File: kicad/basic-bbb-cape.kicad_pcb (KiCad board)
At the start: 2 copper layers, 54.6 x 86.4 mm, 4 parts, among them P1 BeagleBone_Black_Header, P2 BeagleBone_Black_Header, U1 CAT24C32YI-GT3

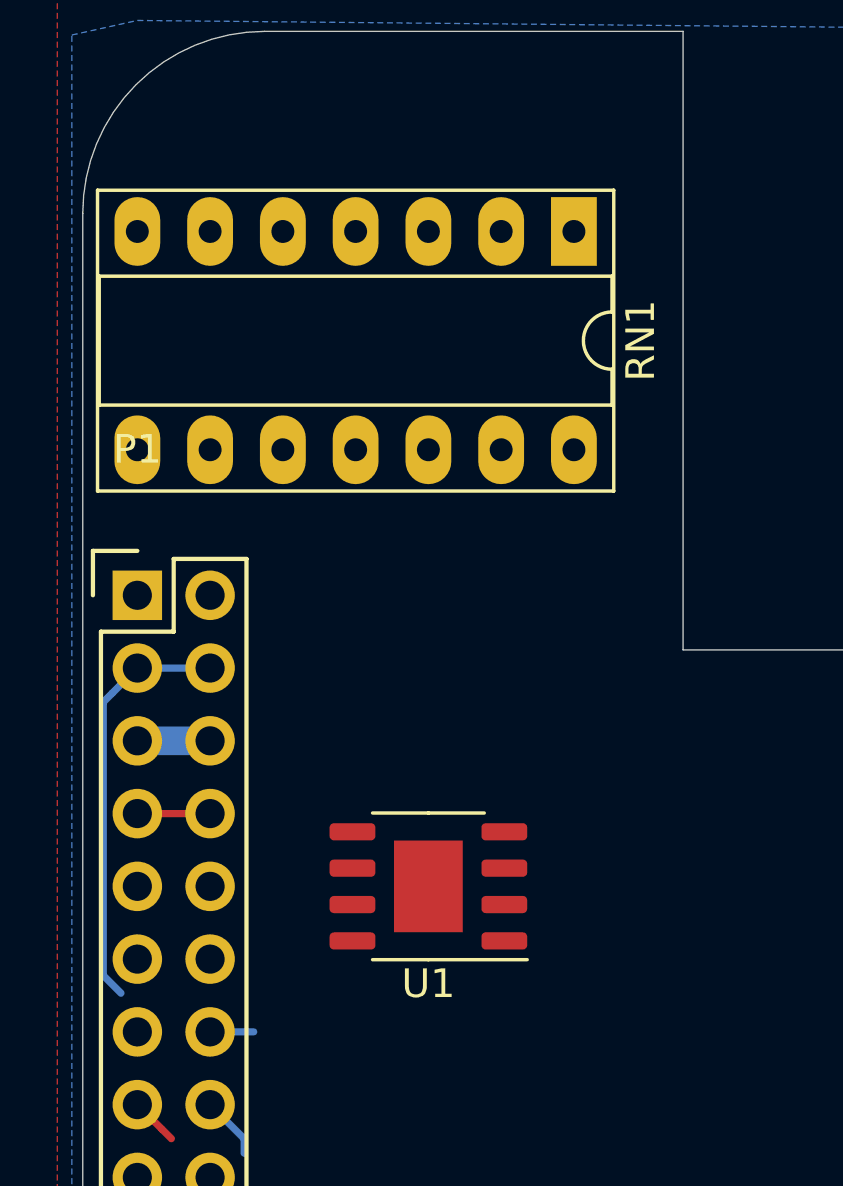
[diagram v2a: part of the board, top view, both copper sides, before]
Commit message: Rotate RP1 and U1 180 degrees
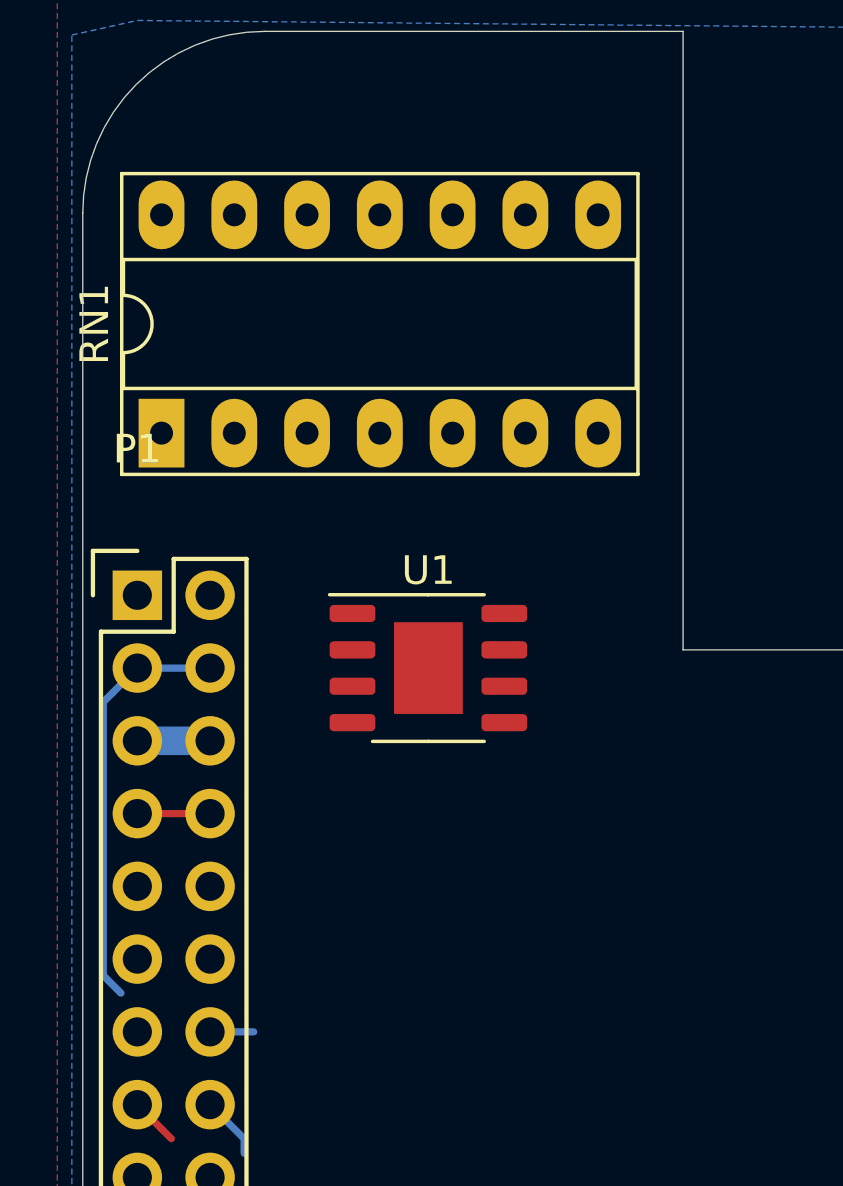
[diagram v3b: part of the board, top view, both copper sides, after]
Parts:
- moved RN1 16.0 mm to (117.2, 56.7), turned to 90 degrees
- moved U1 7.62 mm to (126.5, 64.9), turned to 0 degrees
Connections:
- RN1 pad 1: +3V3 -> Net-(JP1-Pad2)
- RN1 pad 10: Net-(RN1-Pad10) -> +3V3
- RN1 pad 11: unconnected-(RN1-Pad11) -> +3V3
- RN1 pad 12: Net-(RN1-Pad12) -> +3V3
- RN1 pad 13: Net-(JP2-Pad2) -> +3V3
- RN1 pad 14: Net-(JP1-Pad2) -> +3V3
- RN1 pad 2: +3V3 -> Net-(JP2-Pad2)
- RN1 pad 3: +3V3 -> Net-(RN1-Pad3)
- RN1 pad 4: +3V3 -> unconnected-(RN1-Pad4)
- RN1 pad 5: +3V3 -> Net-(RN1-Pad5)
- RN1 pad 6: +3V3 -> I2C2_SDA
- RN1 pad 7: +3V3 -> I2C2_SCL
- RN1 pad 8: I2C2_SDA -> +3V3
- RN1 pad 9: I2C2_SCL -> +3V3
- U1 pad 3: Net-(RN1-Pad12) -> Net-(RN1-Pad3)
- U1 pad 7: Net-(RN1-Pad10) -> Net-(RN1-Pad5)
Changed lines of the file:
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@@
   (net 83 "I2C2_SDA")
   (net 84 "I2C2_SCL")
-  (net 85 "Net-(RN1-Pad10)")
-  (net 86 "unconnected-(RN1-Pad11)")
-  (net 87 "Net-(RN1-Pad12)")
+  (net 85 "Net-(RN1-Pad3)")
+  (net 86 "unconnected-(RN1-Pad4)")
+  (net 87 "Net-(RN1-Pad5)")
   (net 88 "Net-(JP2-Pad2)")
   (net 89 "Net-(JP1-Pad2)")
@@
   )
   (footprint "Package_DIP:DIP-14_W7.62mm_Socket_LongPads" (layer "F.Cu")
-    (at 131.6101 49.6824 -90)
+    (at 117.2151 56.7224 90)
     (descr "14-lead though-hole mounted DIP package, row spacing 7.62 mm (300 mils), Socket, LongPads")
     (tags "THT DIP DIL PDIP 2.54mm 7.62mm 300mil Socket LongPads")
@@
     (fp_line (start 0.635 16.51) (end 0.635 -0.27) (layer "F.Fab") (width 0.1))
     (fp_line (start 0.635 -0.27) (end 1.635 -1.27) (layer "F.Fab") (width 0.1))
-    (pad "1" thru_hole rect (at 0 0 270) (size 2.4 1.6) (drill 0.8) (layers *.Cu *.Mask)
-      (net 1 "+3V3") (pinfunction "R1.1") (pintype "passive"))
-    (pad "2" thru_hole oval (at 0 2.54 270) (size 2.4 1.6) (drill 0.8) (layers *.Cu *.Mask)
-      (net 1 "+3V3") (pinfunction "R2.1") (pintype "passive"))
-    (pad "3" thru_hole oval (at 0 5.08 270) (size 2.4 1.6) (drill 0.8) (layers *.Cu *.Mask)
-      (net 1 "+3V3") (pinfunction "R3.1") (pintype "passive"))
-    (pad "4" thru_hole oval (at 0 7.62 270) (size 2.4 1.6) (drill 0.8) (layers *.Cu *.Mask)
-      (net 1 "+3V3") (pinfunction "R4.1") (pintype "passive"))
-    (pad "5" thru_hole oval (at 0 10.16 270) (size 2.4 1.6) (drill 0.8) (layers *.Cu *.Mask)
-      (net 1 "+3V3") (pinfunction "R5.1") (pintype "passive"))
-    (pad "6" thru_hole oval (at 0 12.7 270) (size 2.4 1.6) (drill 0.8) (layers *.Cu *.Mask)
-      (net 1 "+3V3") (pinfunction "R6.1") (pintype "passive"))
-    (pad "7" thru_hole oval (at 0 15.24 270) (size 2.4 1.6) (drill 0.8) (layers *.Cu *.Mask)
-      (net 1 "+3V3") (pinfunction "R7.1") (pintype "passive"))
-    (pad "8" thru_hole oval (at 7.62 15.24 270) (size 2.4 1.6) (drill 0.8) (layers *.Cu *.Mask)
-      (net 83 "I2C2_SDA") (pinfunction "R7.2") (pintype "passive"))
-    (pad "9" thru_hole oval (at 7.62 12.7 270) (size 2.4 1.6) (drill 0.8) (layers *.Cu *.Mask)
-      (net 84 "I2C2_SCL") (pinfunction "R6.2") (pintype "passive"))
-    (pad "10" thru_hole oval (at 7.62 10.16 270) (size 2.4 1.6) (drill 0.8) (layers *.Cu *.Mask)
-      (net 85 "Net-(RN1-Pad10)") (pinfunction "R5.2") (pintype "passive"))
-    (pad "11" thru_hole oval (at 7.62 7.62 270) (size 2.4 1.6) (drill 0.8) (layers *.Cu *.Mask)
-      (net 86 "unconnected-(RN1-Pad11)") (pinfunction "R4.2") (pintype "passive+no_connect"))
-    (pad "12" thru_hole oval (at 7.62 5.08 270) (size 2.4 1.6) (drill 0.8) (layers *.Cu *.Mask)
-      (net 87 "Net-(RN1-Pad12)") (pinfunction "R3.2") (pintype "passive"))
-    (pad "13" thru_hole oval (at 7.62 2.54 270) (size 2.4 1.6) (drill 0.8) (layers *.Cu *.Mask)
-      (net 88 "Net-(JP2-Pad2)") (pinfunction "R2.2") (pintype "passive"))
-    (pad "14" thru_hole oval (at 7.62 0 270) (size 2.4 1.6) (drill 0.8) (layers *.Cu *.Mask)
-      (net 89 "Net-(JP1-Pad2)") (pinfunction "R1.2") (pintype "passive"))
+    (pad "1" thru_hole rect (at 0 0 90) (size 2.4 1.6) (drill 0.8) (layers *.Cu *.Mask)
+      (net 89 "Net-(JP1-Pad2)") (pinfunction "R1.1") (pintype "passive"))
+    (pad "2" thru_hole oval (at 0 2.54 90) (size 2.4 1.6) (drill 0.8) (layers *.Cu *.Mask)
+      (net 88 "Net-(JP2-Pad2)") (pinfunction "R2.1") (pintype "passive"))
+    (pad "3" thru_hole oval (at 0 5.08 90) (size 2.4 1.6) (drill 0.8) (layers *.Cu *.Mask)
+      (net 85 "Net-(RN1-Pad3)") (pinfunction "R3.1") (pintype "passive"))
+    (pad "4" thru_hole oval (at 0 7.62 90) (size 2.4 1.6) (drill 0.8) (layers *.Cu *.Mask)
+      (net 86 "unconnected-(RN1-Pad4)") (pinfunction "R4.1") (pintype "passive"))
+    (pad "5" thru_hole oval (at 0 10.16 90) (size 2.4 1.6) (drill 0.8) (layers *.Cu *.Mask)
+      (net 87 "Net-(RN1-Pad5)") (pinfunction "R5.1") (pintype "passive"))
+    (pad "6" thru_hole oval (at 0 12.7 90) (size 2.4 1.6) (drill 0.8) (layers *.Cu *.Mask)
+      (net 83 "I2C2_SDA") (pinfunction "R6.1") (pintype "passive"))
+    (pad "7" thru_hole oval (at 0 15.24 90) (size 2.4 1.6) (drill 0.8) (layers *.Cu *.Mask)
+      (net 84 "I2C2_SCL") (pinfunction "R7.1") (pintype "passive"))
+    (pad "8" thru_hole oval (at 7.62 15.24 90) (size 2.4 1.6) (drill 0.8) (layers *.Cu *.Mask)
+      (net 1 "+3V3") (pinfunction "R7.2") (pintype "passive"))
+    (pad "9" thru_hole oval (at 7.62 12.7 90) (size 2.4 1.6) (drill 0.8) (layers *.Cu *.Mask)
+      (net 1 "+3V3") (pinfunction "R6.2") (pintype "passive"))
+    (pad "10" thru_hole oval (at 7.62 10.16 90) (size 2.4 1.6) (drill 0.8) (layers *.Cu *.Mask)
+      (net 1 "+3V3") (pinfunction "R5.2") (pintype "passive"))
+    (pad "11" thru_hole oval (at 7.62 7.62 90) (size 2.4 1.6) (drill 0.8) (layers *.Cu *.Mask)
+      (net 1 "+3V3") (pinfunction "R4.2") (pintype "passive"))
+    (pad "12" thru_hole oval (at 7.62 5.08 90) (size 2.4 1.6) (drill 0.8) (layers *.Cu *.Mask)
+      (net 1 "+3V3") (pinfunction "R3.2") (pintype "passive"))
+    (pad "13" thru_hole oval (at 7.62 2.54 90) (size 2.4 1.6) (drill 0.8) (layers *.Cu *.Mask)
+      (net 1 "+3V3") (pinfunction "R2.2") (pintype "passive"))
+    (pad "14" thru_hole oval (at 7.62 0 90) (size 2.4 1.6) (drill 0.8) (layers *.Cu *.Mask)
+      (net 1 "+3V3") (pinfunction "R1.2") (pintype "passive"))
     (model "${KICAD6_3DMODEL_DIR}/Package_DIP.3dshapes/DIP-14_W7.62mm_Socket.wrl"
       (offset (xyz 0 0 0))
@@
   )
   (footprint "Package_SO:HTSOP-8-1EP_3.9x4.9mm_P1.27mm_EP2.4x3.2mm" (layer "F.Cu")
-    (at 126.5301 72.5424 180)
+    (at 126.5301 64.9224)
     (descr "HTSOP, 8 Pin (https://media.digikey.com/pdf/Data%20Sheets/Rohm%20PDFs/BD9G341EFJ.pdf), generated with kicad-footprint-generator ipc_gullwing_generator.py")
     (tags "HTSOP SO")
@@
     (fp_line (start 1.95 -2.45) (end 1.95 2.45) (layer "F.Fab") (width 0.1))
     (fp_line (start -0.975 -2.45) (end 1.95 -2.45) (layer "F.Fab") (width 0.1))
-    (pad "" smd roundrect (at 0.6 -0.8 180) (size 0.97 1.29) (layers "F.Paste") (roundrect_rratio 0.25))
-    (pad "" smd roundrect (at -0.6 -0.8 180) (size 0.97 1.29) (layers "F.Paste") (roundrect_rratio 0.25))
-    (pad "" smd roundrect (at 0.6 0.8 180) (size 0.97 1.29) (layers "F.Paste") (roundrect_rratio 0.25))
-    (pad "" smd roundrect (at -0.6 0.8 180) (size 0.97 1.29) (layers "F.Paste") (roundrect_rratio 0.25))
-    (pad "1" smd roundrect (at -2.65 -1.905 180) (size 1.6 0.6) (layers "F.Cu" "F.Paste" "F.Mask") (roundrect_rratio 0.25)
+    (pad "" smd roundrect (at 0.6 -0.8) (size 0.97 1.29) (layers "F.Paste") (roundrect_rratio 0.25))
+    (pad "" smd roundrect (at -0.6 -0.8) (size 0.97 1.29) (layers "F.Paste") (roundrect_rratio 0.25))
+    (pad "" smd roundrect (at 0.6 0.8) (size 0.97 1.29) (layers "F.Paste") (roundrect_rratio 0.25))
+    (pad "" smd roundrect (at -0.6 0.8) (size 0.97 1.29) (layers "F.Paste") (roundrect_rratio 0.25))
+    (pad "1" smd roundrect (at -2.65 -1.905) (size 1.6 0.6) (layers "F.Cu" "F.Paste" "F.Mask") (roundrect_rratio 0.25)
       (net 89 "Net-(JP1-Pad2)") (pinfunction "A0") (pintype "input"))
-    (pad "2" smd roundrect (at -2.65 -0.635 180) (size 1.6 0.6) (layers "F.Cu" "F.Paste" "F.Mask") (roundrect_rratio 0.25)
+    (pad "2" smd roundrect (at -2.65 -0.635) (size 1.6 0.6) (layers "F.Cu" "F.Paste" "F.Mask") (roundrect_rratio 0.25)
       (net 88 "Net-(JP2-Pad2)") (pinfunction "A1") (pintype "input"))
-    (pad "3" smd roundrect (at -2.65 0.635 180) (size 1.6 0.6) (layers "F.Cu" "F.Paste" "F.Mask") (roundrect_rratio 0.25)
-      (net 87 "Net-(RN1-Pad12)") (pinfunction "A2") (pintype "input"))
-    (pad "4" smd roundrect (at -2.65 1.905 180) (size 1.6 0.6) (layers "F.Cu" "F.Paste" "F.Mask") (roundrect_rratio 0.25)
+    (pad "3" smd roundrect (at -2.65 0.635) (size 1.6 0.6) (layers "F.Cu" "F.Paste" "F.Mask") (roundrect_rratio 0.25)
+      (net 85 "Net-(RN1-Pad3)") (pinfunction "A2") (pintype "input"))
+    (pad "4" smd roundrect (at -2.65 1.905) (size 1.6 0.6) (layers "F.Cu" "F.Paste" "F.Mask") (roundrect_rratio 0.25)
       (net 90 "GNDD") (pinfunction "GND") (pintype "power_in"))
-    (pad "5" smd roundrect (at 2.65 1.905 180) (size 1.6 0.6) (layers "F.Cu" "F.Paste" "F.Mask") (roundrect_rratio 0.25)
+    (pad "5" smd roundrect (at 2.65 1.905) (size 1.6 0.6) (layers "F.Cu" "F.Paste" "F.Mask") (roundrect_rratio 0.25)
       (net 83 "I2C2_SDA") (pinfunction "SDA") (pintype "bidirectional"))
-    (pad "6" smd roundrect (at 2.65 0.635 180) (size 1.6 0.6) (layers "F.Cu" "F.Paste" "F.Mask") (roundrect_rratio 0.25)
+    (pad "6" smd roundrect (at 2.65 0.635) (size 1.6 0.6) (layers "F.Cu" "F.Paste" "F.Mask") (roundrect_rratio 0.25)
       (net 84 "I2C2_SCL") (pinfunction "SCL") (pintype "input"))
-    (pad "7" smd roundrect (at 2.65 -0.635 180) (size 1.6 0.6) (layers "F.Cu" "F.Paste" "F.Mask") (roundrect_rratio 0.25)
-      (net 85 "Net-(RN1-Pad10)") (pinfunction "WP") (pintype "input"))
-    (pad "8" smd roundrect (at 2.65 -1.905 180) (size 1.6 0.6) (layers "F.Cu" "F.Paste" "F.Mask") (roundrect_rratio 0.25)
+    (pad "7" smd roundrect (at 2.65 -0.635) (size 1.6 0.6) (layers "F.Cu" "F.Paste" "F.Mask") (roundrect_rratio 0.25)
+      (net 87 "Net-(RN1-Pad5)") (pinfunction "WP") (pintype "input"))
+    (pad "8" smd roundrect (at 2.65 -1.905) (size 1.6 0.6) (layers "F.Cu" "F.Paste" "F.Mask") (roundrect_rratio 0.25)
       (net 1 "+3V3") (pinfunction "VCC") (pintype "power_in"))
-    (pad "9" smd rect (at 0 0 180) (size 2.4 3.2) (layers "F.Cu" "F.Mask"))
+    (pad "9" smd rect (at 0 0) (size 2.4 3.2) (layers "F.Cu" "F.Mask"))
     (model "${KICAD6_3DMODEL_DIR}/Package_SO.3dshapes/HTSOP-8-1EP_3.9x4.9mm_P1.27mm_EP2.4x3.2mm.wrl"
       (offset (xyz 0 0 0))

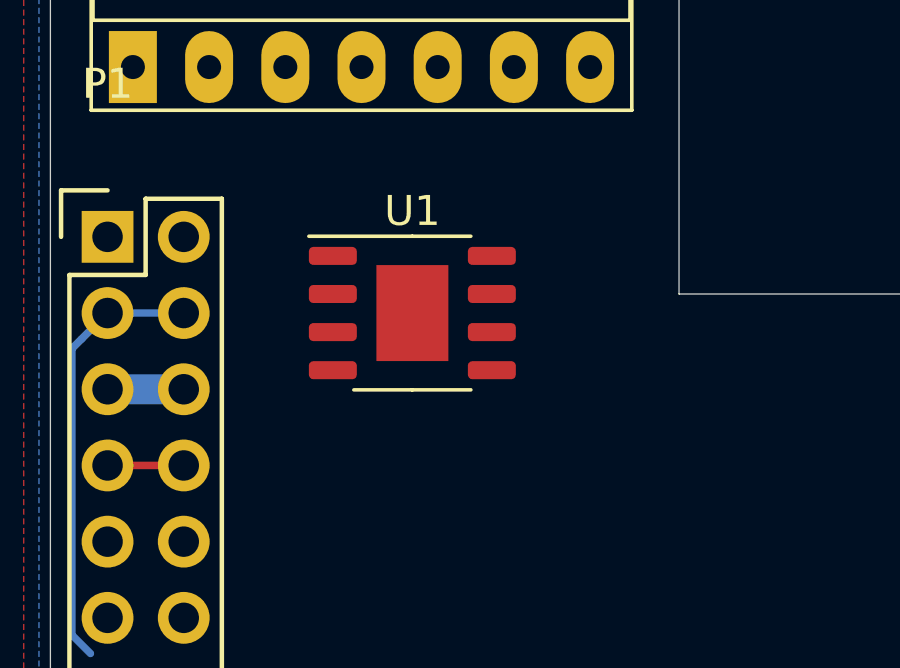
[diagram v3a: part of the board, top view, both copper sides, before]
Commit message: Add solder jumper to PCB
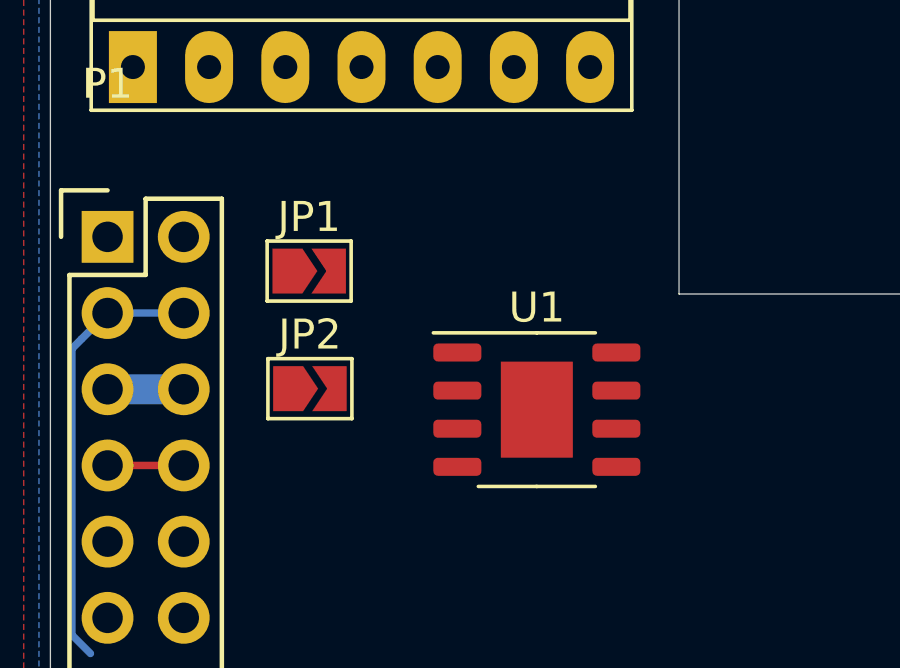
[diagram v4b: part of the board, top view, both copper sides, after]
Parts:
- added JP1: SolderJumper_2_Open, Jumper:SolderJumper-2_P1.3mm_Open_TrianglePad1.0x1.5mm, F.Cu at (123.1, 63.5)
- added JP2: SolderJumper_2_Open, Jumper:SolderJumper-2_P1.3mm_Open_TrianglePad1.0x1.5mm, F.Cu at (123.1, 67.4)
- moved U1 5.25 mm to (130.7, 68.1)
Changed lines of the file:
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@@
     )
+  )
+  (footprint "Jumper:SolderJumper-2_P1.3mm_Open_TrianglePad1.0x1.5mm" (layer "F.Cu")
+    (at 123.1151 67.4424)
+    (descr "SMD Solder Jumper, 1x1.5mm Triangular Pads, 0.3mm gap, open")
+    (tags "solder jumper open")
+    (property "Sheetfile" "basic-bbb-cape.kicad_sch")
+    (property "Sheetname" "")
+    (attr exclude_from_pos_files)
+    (fp_text reference "JP2" (at 0 -1.8) (layer "F.SilkS")
+      (effects (font (size 1 1) (thickness 0.15)))
+    )
+    (fp_text value "SolderJumper_2_Open" (at 0 1.9) (layer "F.Fab") hide
+      (effects (font (size 1 1) (thickness 0.15)))
+    )
+    (fp_line (start -1.4 1) (end -1.4 -1) (layer "F.SilkS") (width 0.12))
+    (fp_line (start 1.4 1) (end -1.4 1) (layer "F.SilkS") (width 0.12))
+    (fp_line (start -1.4 -1) (end 1.4 -1) (layer "F.SilkS") (width 0.12))
+    (fp_line (start 1.4 -1) (end 1.4 1) (layer "F.SilkS") (width 0.12))
+    (fp_line (start 1.65 1.25) (end 1.65 -1.25) (layer "F.CrtYd") (width 0.05))
+    (fp_line (start 1.65 1.25) (end -1.65 1.25) (layer "F.CrtYd") (width 0.05))
+    (fp_line (start -1.65 -1.25) (end -1.65 1.25) (layer "F.CrtYd") (width 0.05))
+    (fp_line (start -1.65 -1.25) (end 1.65 -1.25) (layer "F.CrtYd") (width 0.05))
+    (pad "1" smd custom (at -0.725 0) (size 0.3 0.3) (layers "F.Cu" "F.Mask")
+      (net 90 "GNDD") (pinfunction "A") (pintype "passive") (zone_connect 2)
+      (options (clearance outline) (anchor rect))
+      (primitives
+        (gr_poly (pts
+            (xy 1 0)
+            (xy 0.5 0.75)
+            (xy -0.5 0.75)
+            (xy -0.5 -0.75)
+            (xy 0.5 -0.75)
+          ) (width 0) (fill yes))
+      ))
+    (pad "2" smd custom (at 0.725 0) (size 0.3 0.3) (layers "F.Cu" "F.Mask")
+      (net 88 "Net-(JP2-Pad2)") (pinfunction "B") (pintype "passive") (zone_connect 2)
+      (options (clearance outline) (anchor rect))
+      (primitives
+        (gr_poly (pts
+            (xy 0.5 0.75)
+            (xy -0.65 0.75)
+            (xy -0.15 0)
+            (xy -0.65 -0.75)
+            (xy 0.5 -0.75)
+          ) (width 0) (fill yes))
+      ))
   )
   (footprint "Package_DIP:DIP-14_W7.62mm_Socket_LongPads" (layer "F.Cu")
@@
       (net 85 "Net-(RN1-Pad3)") (pinfunction "R3.1") (pintype "passive"))
     (pad "4" thru_hole oval (at 0 7.62 90) (size 2.4 1.6) (drill 0.8) (layers *.Cu *.Mask)
-      (net 86 "unconnected-(RN1-Pad4)") (pinfunction "R4.1") (pintype "passive"))
+      (net 86 "unconnected-(RN1-Pad4)") (pinfunction "R4.1") (pintype "passive+no_connect"))
     (pad "5" thru_hole oval (at 0 10.16 90) (size 2.4 1.6) (drill 0.8) (layers *.Cu *.Mask)
       (net 87 "Net-(RN1-Pad5)") (pinfunction "R5.1") (pintype "passive"))
@@
     )
   )
+  (footprint "Jumper:SolderJumper-2_P1.3mm_Open_TrianglePad1.0x1.5mm" (layer "F.Cu")
+    (at 123.0901 63.5224)
+    (descr "SMD Solder Jumper, 1x1.5mm Triangular Pads, 0.3mm gap, open")
+    (tags "solder jumper open")
+    (property "Sheetfile" "basic-bbb-cape.kicad_sch")
+    (property "Sheetname" "")
+    (attr exclude_from_pos_files)
+    (fp_text reference "JP1" (at 0 -1.8) (layer "F.SilkS")
+      (effects (font (size 1 1) (thickness 0.15)))
+    )
+    (fp_text value "SolderJumper_2_Open" (at 0 1.9) (layer "F.Fab") hide
+      (effects (font (size 1 1) (thickness 0.15)))
+    )
+    (fp_line (start 1.4 -1) (end 1.4 1) (layer "F.SilkS") (width 0.12))
+    (fp_line (start 1.4 1) (end -1.4 1) (layer "F.SilkS") (width 0.12))
+    (fp_line (start -1.4 1) (end -1.4 -1) (layer "F.SilkS") (width 0.12))
+    (fp_line (start -1.4 -1) (end 1.4 -1) (layer "F.SilkS") (width 0.12))
+    (fp_line (start -1.65 -1.25) (end 1.65 -1.25) (layer "F.CrtYd") (width 0.05))
+    (fp_line (start 1.65 1.25) (end -1.65 1.25) (layer "F.CrtYd") (width 0.05))
+    (fp_line (start 1.65 1.25) (end 1.65 -1.25) (layer "F.CrtYd") (width 0.05))
+    (fp_line (start -1.65 -1.25) (end -1.65 1.25) (layer "F.CrtYd") (width 0.05))
+    (pad "1" smd custom (at -0.725 0) (size 0.3 0.3) (layers "F.Cu" "F.Mask")
+      (net 90 "GNDD") (pinfunction "A") (pintype "passive") (zone_connect 2)
+      (options (clearance outline) (anchor rect))
+      (primitives
+        (gr_poly (pts
+            (xy 1 0)
+            (xy 0.5 0.75)
+            (xy -0.5 0.75)
+            (xy -0.5 -0.75)
+            (xy 0.5 -0.75)
+          ) (width 0) (fill yes))
+      ))
+    (pad "2" smd custom (at 0.725 0) (size 0.3 0.3) (layers "F.Cu" "F.Mask")
+      (net 89 "Net-(JP1-Pad2)") (pinfunction "B") (pintype "passive") (zone_connect 2)
+      (options (clearance outline) (anchor rect))
+      (primitives
+        (gr_poly (pts
+            (xy 0.5 0.75)
+            (xy -0.65 0.75)
+            (xy -0.15 0)
+            (xy -0.65 -0.75)
+            (xy 0.5 -0.75)
+          ) (width 0) (fill yes))
+      ))
+  )
   (footprint "Package_SO:HTSOP-8-1EP_3.9x4.9mm_P1.27mm_EP2.4x3.2mm" (layer "F.Cu")
-    (at 126.5301 64.9224)
+    (at 130.6801 68.1424)
     (descr "HTSOP, 8 Pin (https://media.digikey.com/pdf/Data%20Sheets/Rohm%20PDFs/BD9G341EFJ.pdf), generated with kicad-footprint-generator ipc_gullwing_generator.py")
     (tags "HTSOP SO")
